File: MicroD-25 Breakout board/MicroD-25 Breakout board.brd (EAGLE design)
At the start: 160 x 100 mm, 1 part

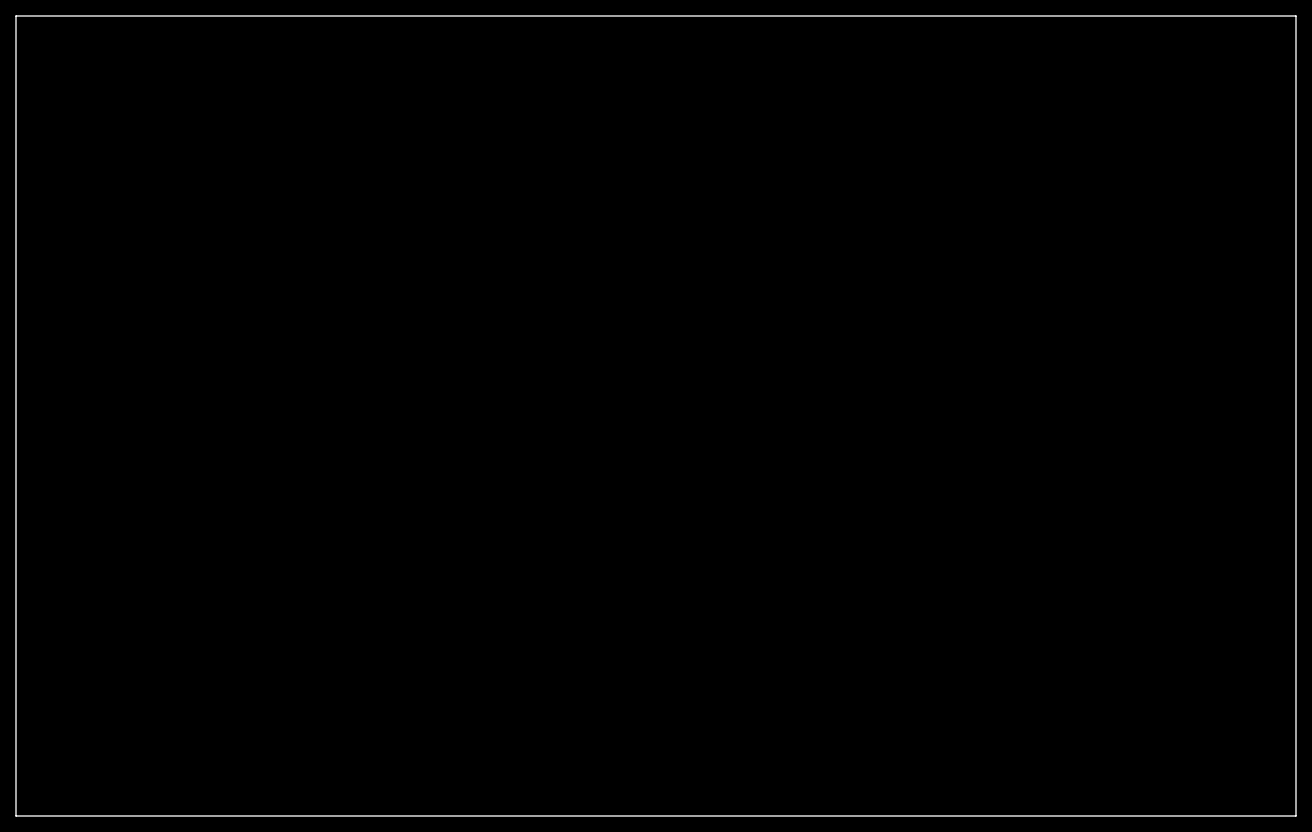
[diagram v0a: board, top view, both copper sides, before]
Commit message: Complete routing of Micro-D25 breakout board. Coordinate with MechE and send to manufacture
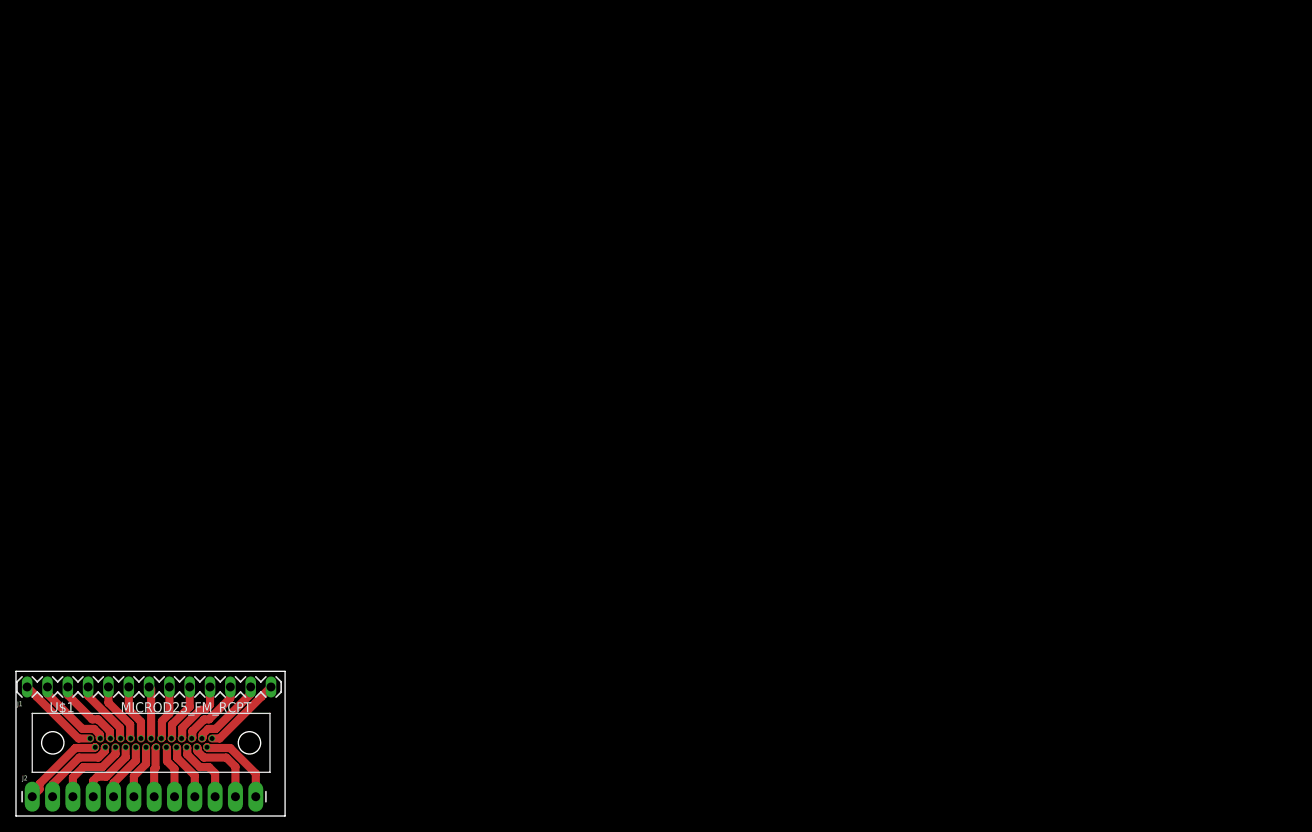
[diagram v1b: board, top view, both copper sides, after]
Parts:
- added J1: (no value), SparkFun-Connectors:1X13-LONGPADS
- added J2: (no value), SparkFun-Connectors:1X12_LONGPADS
- added U$1: MICROD25_FM_RCPT, Braly2:MICROD25_FM_RCPT
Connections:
- new net N$1: J1.13, U$1.PIN1
- new net N$10: J1.4, U$1.PIN19
- new net N$11: J1.3, U$1.PIN21
- new net N$12: J1.2, U$1.PIN23
- new net N$13: J1.1, U$1.PIN25
- new net N$14: J2.12, U$1.PIN2
- new net N$15: J2.11, U$1.PIN4
- new net N$16: J2.10, U$1.PIN6
- new net N$17: J2.9, U$1.PIN8
- new net N$18: J2.8, U$1.PIN10
- new net N$19: J2.7, U$1.PIN12
- new net N$2: J1.12, U$1.PIN3
- new net N$20: J2.6, U$1.PIN14
- new net N$21: J2.5, U$1.PIN16
- new net N$22: J2.4, U$1.PIN18
- new net N$23: J2.3, U$1.PIN20
- new net N$24: J2.2, U$1.PIN22
- new net N$25: J2.1, U$1.PIN24
- new net N$3: J1.11, U$1.PIN5
- new net N$4: J1.10, U$1.PIN7
- new net N$5: J1.9, U$1.PIN9
- new net N$6: J1.8, U$1.PIN11
- new net N$7: J1.7, U$1.PIN13
- new net N$8: J1.6, U$1.PIN15
- new net N$9: J1.5, U$1.PIN17
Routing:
- net N$25: track 0.00 -> 10.8 mm
- net N$13: track 0.00 -> 10.6 mm
- net N$14: track 0.00 -> 10.4 mm
- net N$24: track 0.00 -> 10.3 mm
- net N$1: track 0.00 -> 10.0 mm
- net N$12: track 0.00 -> 10.0 mm
- net N$15: track 0.00 -> 9.82 mm
- net N$23: track 0.00 -> 9.79 mm
- net N$2: track 0.00 -> 9.52 mm
- net N$11: track 0.00 -> 9.08 mm
- net N$3: track 0.00 -> 8.79 mm
- net N$22: track 0.00 -> 8.53 mm
- net N$16: track 0.00 -> 8.33 mm
- net N$4: track 0.00 -> 8.27 mm
- net N$10: track 0.00 -> 8.12 mm
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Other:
- board size 160 x 100 mm -> 33.6 x 18.1 mm
